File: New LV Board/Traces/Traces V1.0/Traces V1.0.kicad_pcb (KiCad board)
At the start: 2 copper layers, 126.6 x 49.2 mm, 15 parts, among them J1 B15B-PH-K-S, J2 B15B-PH-K-S, J3 B15B-PH-K-S, J4 Conn_01x12, J5 VBATT +, J6 Conn_01x12, J7 Conn_01x12, J8 Vs

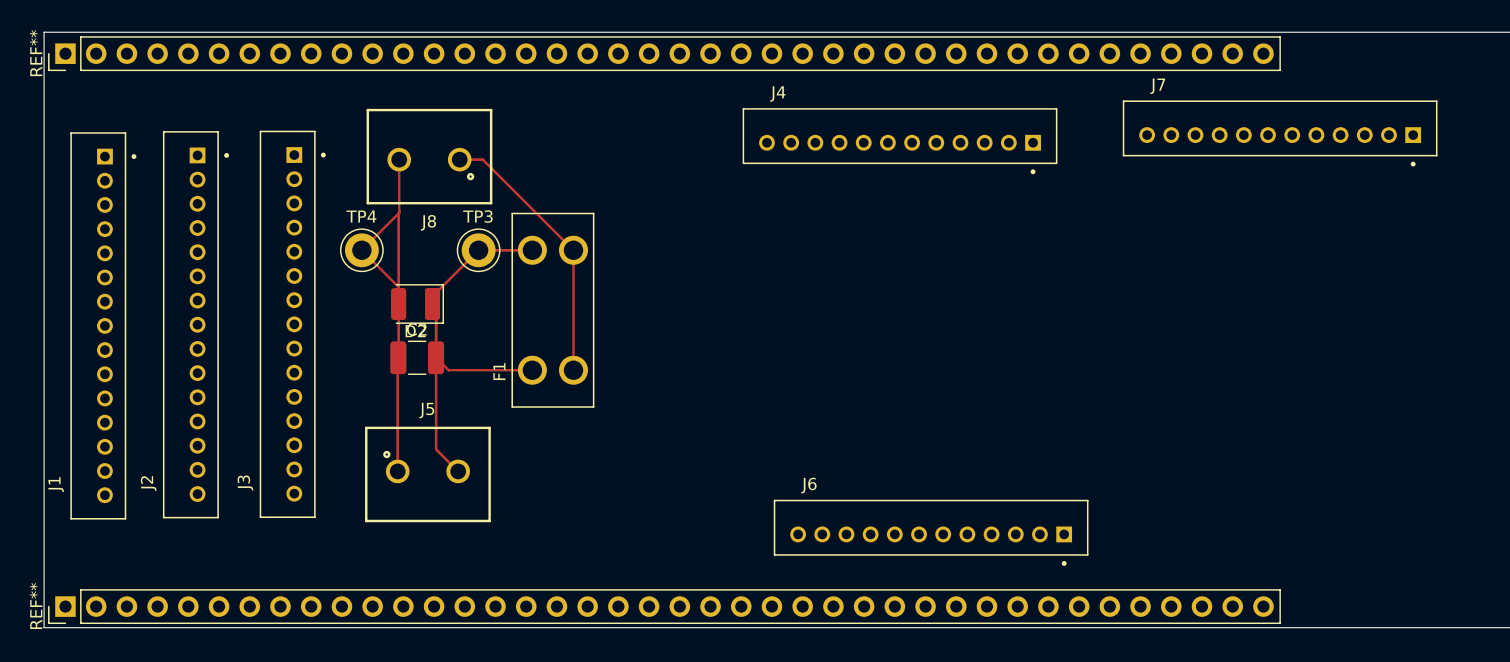
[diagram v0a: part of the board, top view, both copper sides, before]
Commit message: vcu throttle latching connected to traces
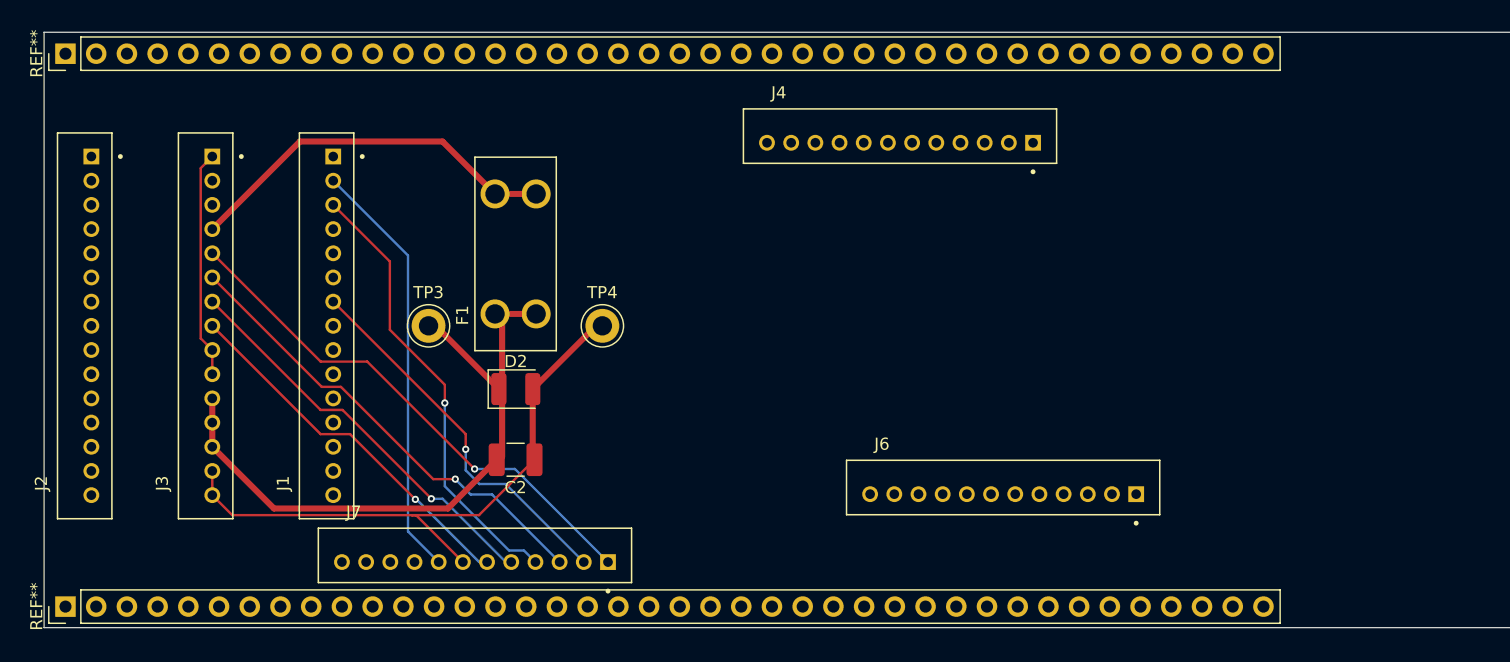
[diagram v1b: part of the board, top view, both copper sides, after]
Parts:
- removed J5: VBATT +, motorsports:691137710002
- removed J8: Vs, motorsports:691137710002
- moved J7 75.4 mm to (79.6, 138.3)
- moved TP4 20.8 mm to (90.1, 119.3)
- moved J1 18.9 mm to (67.3, 119.3)
- moved C2 11.7 mm to (82.9, 130.4), turned to 180 degrees
- moved D2 10.9 mm to (83.0, 124.5), turned to 0 degrees
- moved J2 8.78 mm to (47.3, 119.3)
- moved TP3 7.50 mm to (75.7, 119.3)
- moved J6 6.82 mm to (123.3, 132.6)
- moved J3 6.78 mm to (57.3, 119.3)
- moved F1 5.59 mm to (82.9, 113.3)
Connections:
- F1 pad 3: Net-(F1-Pad3) -> Net-(J4-Pin_3)
- F1 pad 4: Net-(F1-Pad3) -> Net-(J4-Pin_3)
- J1 pad 7: Net-(J7-Pin_6) -> Net-(J7-Pin_2)
- J3 pad 1: Net-(J7-Pin_5) -> Net-(J3-Pad1)
- J3 pad 10: unconnected-(J3-Pad10) -> Net-(J3-Pad1)
- J3 pad 11: unconnected-(J3-Pad11) -> Net-(D2-K)
- J3 pad 12: unconnected-(J3-Pad12) -> Net-(D2-K)
- J3 pad 13: unconnected-(J3-Pad13) -> Net-(D2-K)
- J3 pad 14: unconnected-(J3-Pad14) -> Net-(D2-A)
- J3 pad 15: unconnected-(J3-Pad15) -> Net-(D2-A)
- J3 pad 2: Net-(J4-Pin_3) -> unconnected-(J3-Pad2)
- J3 pad 4: Net-(J7-Pin_12) -> Net-(J4-Pin_3)
- J3 pad 5: Net-(J7-Pin_10) -> Net-(J7-Pin_1)
- J3 pad 6: unconnected-(J3-Pad6) -> Net-(J7-Pin_3)
- J3 pad 7: unconnected-(J3-Pad7) -> Net-(J7-Pin_5)
- J3 pad 8: unconnected-(J3-Pad8) -> Net-(J7-Pin_6)
- J3 pad 9: unconnected-(J3-Pad9) -> Net-(J3-Pad1)
- J4 pad 6: Net-(J4-Pin_6) -> Net-(D2-A)
- J4 pad 8: Net-(J4-Pin_6) -> Net-(D2-A)
- J6 pad 7: Net-(J4-Pin_6) -> Net-(D2-A)
- J7 pad 1: Net-(J4-Pin_10) -> Net-(J7-Pin_1)
- J7 pad 10: Net-(J7-Pin_10) -> unconnected-(J7-Pin_10-Pad10)
- J7 pad 12: Net-(J7-Pin_12) -> unconnected-(J7-Pin_12-Pad12)
- J7 pad 2: Net-(J4-Pin_10) -> Net-(J7-Pin_2)
- J7 pad 3: Net-(J4-Pin_6) -> Net-(J7-Pin_3)
- J7 pad 4: Net-(J7-Pin_10) -> Net-(J4-Pin_7)
- J7 pad 7: Net-(J4-Pin_10) -> Net-(D2-A)
- J7 pad 8: Net-(J4-Pin_7) -> Net-(J4-Pin_10)
- J7 pad 9: Net-(J4-Pin_6) -> unconnected-(J7-Pin_9-Pad9)
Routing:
- net Net-(J7-Pin_1): track 0.00 -> 43.5 mm, vias 0 -> 1
- net Net-(J7-Pin_3): track 0.00 -> 38.5 mm, vias 0 -> 1
- net Net-(J4-Pin_7): track 0.00 -> 37.2 mm, vias 0 -> 1
- net Net-(J4-Pin_10): track 0.00 -> 35.1 mm
- net Net-(J7-Pin_5): track 0.00 -> 33.6 mm, vias 0 -> 1
- net Net-(J4-Pin_3): track 0.00 -> 31.6 mm
- net Net-(J7-Pin_2): track 0.00 -> 31.4 mm, vias 0 -> 1
- net Net-(J7-Pin_6): track 0.00 -> 30.8 mm, vias 0 -> 1
- net Net-(F1-Pad3): track 22.4 -> 0.00 mm
- net Net-(J3-Pad1): track 0.00 -> 18.8 mm
- net Net-(D2-K): track 37.9 -> 55.0 mm
- net Net-(D2-A): track 35.9 -> 50.9 mm

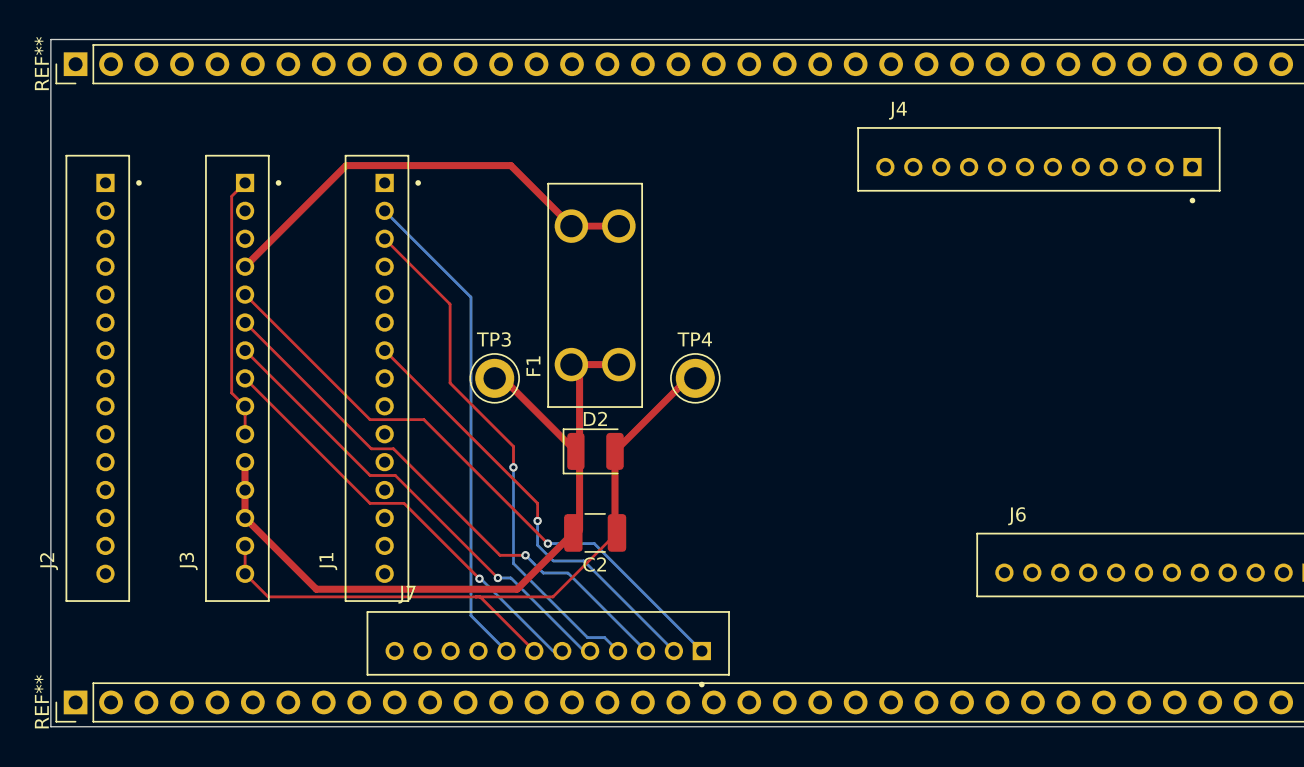
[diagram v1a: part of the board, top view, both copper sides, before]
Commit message: traces board changed to add VCU MPR - 5V connections
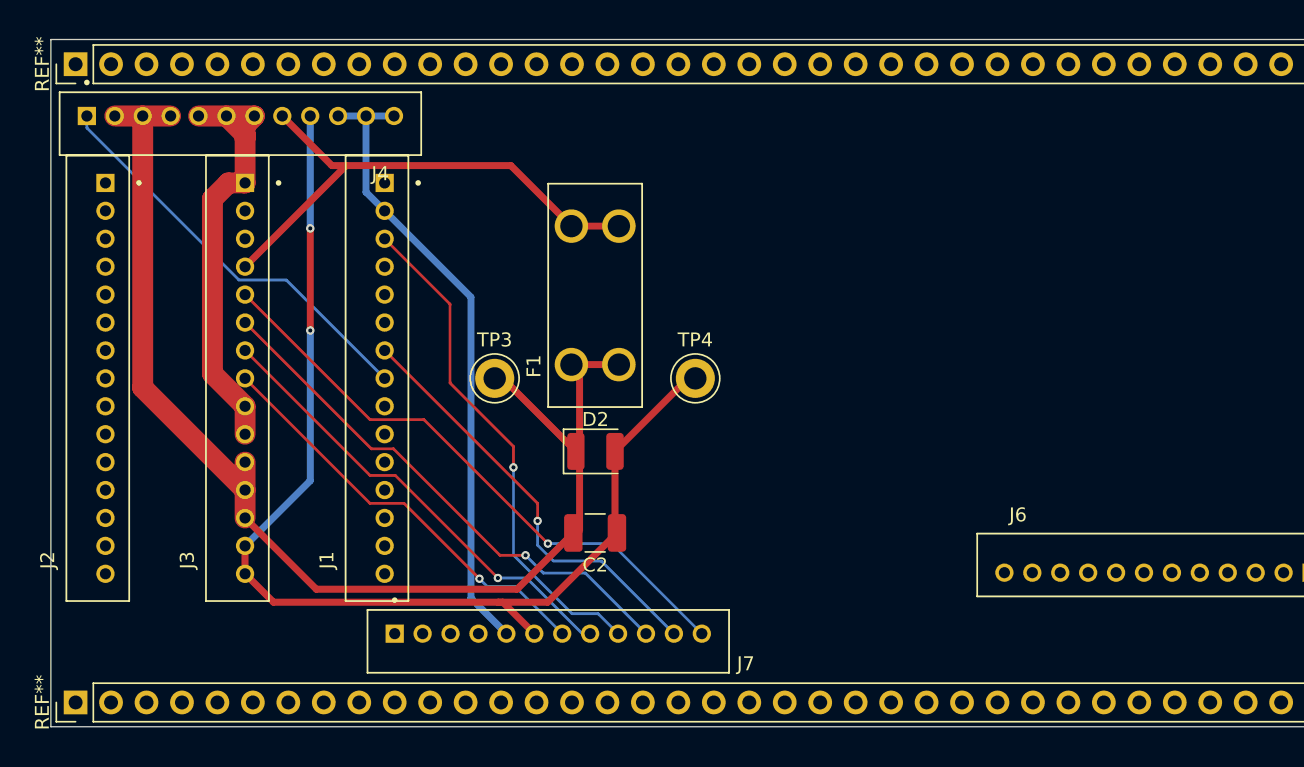
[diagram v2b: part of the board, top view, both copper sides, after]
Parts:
- moved J4 57.3 mm to (57.5, 101.0), turned to 180 degrees
- moved J7 0.14 mm to (79.6, 138.1), turned to 180 degrees
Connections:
- F1 pad 3: Net-(J4-Pin_3) -> Net-(J4-Pin_8)
- F1 pad 4: Net-(J4-Pin_3) -> Net-(J4-Pin_8)
- J1 pad 1: Net-(J4-Pin_4) -> Net-(J6-Pin_11)
- J1 pad 10: Net-(J4-Pin_1) -> Net-(J6-Pin_8)
- J1 pad 11: Net-(J4-Pin_2) -> Net-(J6-Pin_9)
- J1 pad 12: Net-(J6-Pin_5) -> Net-(J6-Pin_7)
- J1 pad 14: Net-(J6-Pin_2) -> Net-(J6-Pin_4)
- J1 pad 15: Net-(J6-Pin_3) -> Net-(J6-Pin_5)
- J1 pad 3: Net-(J4-Pin_7) -> Net-(J6-Pin_12)
- J1 pad 7: Net-(J7-Pin_2) -> Net-(J7-Pin_11)
- J1 pad 8: Net-(J6-Pin_1) -> Net-(J4-Pin_1)
- J1 pad 9: Net-(J4-Pin_5) -> Net-(J6-Pin_10)
- J3 pad 1: Net-(J3-Pad1) -> Net-(J4-Pin_5)
- J3 pad 10: Net-(J3-Pad1) -> Net-(J4-Pin_5)
- J3 pad 4: Net-(J4-Pin_3) -> Net-(J4-Pin_8)
- J3 pad 5: Net-(J7-Pin_1) -> Net-(J7-Pin_12)
- J3 pad 6: Net-(J7-Pin_3) -> Net-(J7-Pin_10)
- J3 pad 7: Net-(J7-Pin_5) -> Net-(J7-Pin_8)
- J3 pad 8: Net-(J7-Pin_6) -> Net-(J7-Pin_7)
- J3 pad 9: Net-(J3-Pad1) -> Net-(J4-Pin_5)
- J4 pad 2: Net-(J4-Pin_2) -> Net-(D2-K)
- J4 pad 3: Net-(J4-Pin_3) -> Net-(D2-K)
- J4 pad 4: Net-(J4-Pin_4) -> Net-(D2-K)
- J4 pad 6: Net-(D2-A) -> Net-(J4-Pin_5)
- J4 pad 7: Net-(J4-Pin_7) -> Net-(J4-Pin_5)
- J4 pad 8: Net-(D2-A) -> Net-(J4-Pin_8)
- J4 pad 9: Net-(J4-Pin_3) -> Net-(D2-A)
- J6 pad 1: Net-(J6-Pin_1) -> Net-(J4-Pin_5)
- J6 pad 10: unconnected-(J6-Pin_10-Pad10) -> Net-(J6-Pin_10)
- J6 pad 11: unconnected-(J6-Pin_11-Pad11) -> Net-(J6-Pin_11)
- J6 pad 12: unconnected-(J6-Pin_12-Pad12) -> Net-(J6-Pin_12)
- J6 pad 2: Net-(J6-Pin_2) -> Net-(J4-Pin_8)
- J6 pad 3: Net-(J6-Pin_3) -> Net-(D2-A)
- J6 pad 4: Net-(J4-Pin_3) -> Net-(J6-Pin_4)
- J6 pad 7: Net-(D2-A) -> Net-(J6-Pin_7)
- J6 pad 8: Net-(J4-Pin_7) -> Net-(J6-Pin_8)
- J6 pad 9: unconnected-(J6-Pin_9-Pad9) -> Net-(J6-Pin_9)
- J7 pad 1: Net-(J7-Pin_1) -> unconnected-(J7-Pin_1-Pad1)
- J7 pad 10: unconnected-(J7-Pin_10-Pad10) -> Net-(J7-Pin_10)
- J7 pad 11: unconnected-(J7-Pin_11-Pad11) -> Net-(J7-Pin_11)
- J7 pad 12: unconnected-(J7-Pin_12-Pad12) -> Net-(J7-Pin_12)
- J7 pad 2: Net-(J7-Pin_2) -> unconnected-(J7-Pin_2-Pad2)
- J7 pad 3: Net-(J7-Pin_3) -> unconnected-(J7-Pin_3-Pad3)
- J7 pad 4: Net-(J4-Pin_7) -> unconnected-(J7-Pin_4-Pad4)
- J7 pad 5: Net-(J7-Pin_5) -> Net-(J4-Pin_10)
- J7 pad 6: Net-(J7-Pin_6) -> Net-(D2-A)
- J7 pad 7: Net-(D2-A) -> Net-(J7-Pin_7)
- J7 pad 8: Net-(J4-Pin_10) -> Net-(J7-Pin_8)
- J7 pad 9: unconnected-(J7-Pin_9-Pad9) -> Net-(J6-Pin_12)
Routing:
- net Net-(J7-Pin_1): track 43.5 -> 0.00 mm, vias 1 -> 0
- net Net-(J7-Pin_12): track 0.00 -> 43.0 mm, vias 0 -> 1
- net Net-(J7-Pin_3): track 38.5 -> 0.00 mm, vias 1 -> 0
- net Net-(J7-Pin_10): track 0.00 -> 38.0 mm, vias 0 -> 1
- net Net-(J4-Pin_8): track 0.00 -> 37.6 mm
- net Net-(J4-Pin_7): track 37.2 -> 0.00 mm, vias 1 -> 0
- net Net-(J6-Pin_12): track 0.00 -> 36.3 mm, vias 0 -> 1
- net Net-(D2-K): track 55.0 -> 88.8 mm
- net Net-(J7-Pin_5): track 33.6 -> 0.00 mm, vias 1 -> 0
- net Net-(J7-Pin_8): track 0.00 -> 33.1 mm, vias 0 -> 1
- net Net-(J4-Pin_5): track 0.00 -> 31.8 mm
- net Net-(J4-Pin_3): track 31.6 -> 0.00 mm
- net Net-(J7-Pin_2): track 31.4 -> 0.00 mm, vias 1 -> 0
- net Net-(J7-Pin_11): track 0.00 -> 30.9 mm, vias 0 -> 1
- net Net-(J7-Pin_6): track 30.8 -> 0.00 mm, vias 1 -> 0
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
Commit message: TRACES IS DONE
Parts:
- moved J6 35.2 mm to (108.4, 100.8), turned to 180 degrees
- moved J1 20.1 mm to (47.3, 121.3)
- moved J2 20.1 mm to (67.3, 121.3)
- moved REF** 5.08 mm to (45.7, 147.6)
- moved J7 4.90 mm to (79.6, 143.0)
- moved D2 2.02 mm to (83.0, 126.5)
- moved F1 2.02 mm to (82.9, 115.4)
- moved C2 2.02 mm to (82.9, 132.4)
- moved J3 2.02 mm to (57.3, 121.3)
- moved TP3 2.02 mm to (75.7, 121.3)
- moved TP4 2.02 mm to (90.1, 121.3)
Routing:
- net Net-(J6-Pin_10): track 0.00 -> 116.7 mm
- net Net-(J6-Pin_9): track 0.00 -> 106.5 mm, vias 0 -> 2
- net Net-(J6-Pin_8): track 0.00 -> 105.3 mm, vias 0 -> 2
- net Net-(J6-Pin_12): track 36.3 -> 130.9 mm, vias 1 -> 0
- net Net-(J6-Pin_7): track 0.00 -> 88.8 mm, vias 0 -> 1
- net Net-(J6-Pin_6): track 0.00 -> 87.4 mm, vias 0 -> 1
- net Net-(J6-Pin_5): track 0.00 -> 86.8 mm, vias 0 -> 1
- net Net-(J6-Pin_4): track 0.00 -> 82.9 mm, vias 0 -> 1
- net Net-(J6-Pin_11): track 0.00 -> 81.4 mm
- net Net-(J4-Pin_5): track 31.8 -> 72.6 mm
- net Net-(J4-Pin_10): track 45.2 -> 81.6 mm, vias 0 -> 2
- net Net-(J7-Pin_11): track 30.9 -> 63.1 mm
- net Net-(D2-A): track 81.6 -> 111.8 mm, vias 2 -> 1
- net Net-(J7-Pin_10): track 38.0 -> 67.6 mm, vias 1 -> 0
- net Net-(J7-Pin_12): track 43.0 -> 66.6 mm, vias 1 -> 2
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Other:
- board size 126.6 x 49.2 mm -> 103.1 x 54.3 mm

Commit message: rotated JST PH 12 it may not match the schematic exactly but it is correct electrically.
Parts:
- moved J7 1.02 mm to (79.6, 142.0), turned to 0 degrees
- moved J1 0.98 mm to (48.3, 121.3), turned to -90 degrees
- moved J3 0.98 mm to (58.3, 121.3), turned to -90 degrees
- moved J2 0.98 mm to (68.3, 121.3), turned to -90 degrees
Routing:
- net Net-(J4-Pin_5): track 72.6 -> 179.8 mm
- net Net-(J7-Pin_10): track 67.6 -> 0.00 mm
- net Net-(J7-Pin_12): track 66.6 -> 0.00 mm, vias 2 -> 0
- net Net-(D2-K): track 90.0 -> 156.6 mm, vias 0 -> 2
- net Net-(J7-Pin_8): track 39.5 -> 0.00 mm

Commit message: No significant changes just random kicad BS
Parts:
- moved D2 5.91 mm to (85.5, 121.2)
- moved F1 5.91 mm to (85.5, 110.0)
- moved J6 5.91 mm to (110.9, 95.5)
- moved J7 5.91 mm to (82.1, 136.7)
- moved REF** 5.91 mm to (48.3, 142.2)
- moved REF** 5.91 mm to (48.3, 91.4)
- moved C2 5.91 mm to (85.5, 127.0)
- moved J2 5.91 mm to (70.8, 116.0)
- moved TP4 5.91 mm to (92.7, 116.0)
- moved J1 5.91 mm to (50.8, 116.0)
- moved J3 5.91 mm to (60.8, 116.0)
- moved J4 5.91 mm to (60.1, 95.7)
- moved TP3 5.91 mm to (78.3, 116.0)
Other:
- board size 103.1 x 54.3 mm -> 103.1 x 53.3 mm

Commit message: Gerbers for Traces board
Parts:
- moved D2 5.91 mm to (83.0, 126.5)
- moved F1 5.91 mm to (82.9, 115.4)
- moved J6 5.91 mm to (108.4, 100.8)
- moved J7 5.91 mm to (79.6, 142.0)
- moved REF** 5.91 mm to (45.7, 147.6)
- moved REF** 5.91 mm to (45.7, 96.8)
- moved C2 5.91 mm to (82.9, 132.4)
- moved J2 5.91 mm to (68.3, 121.3)
- moved TP4 5.91 mm to (90.1, 121.3)
- moved J1 5.91 mm to (48.3, 121.3)
- moved J3 5.91 mm to (58.3, 121.3)
- moved J4 5.91 mm to (57.5, 101.0)
- moved TP3 5.91 mm to (75.7, 121.3)
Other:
- board size 103.1 x 53.3 mm -> 103.1 x 54.3 mm
- board text added: "Traces V1.0 | J.E. Nov '25"

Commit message: traces fixing pt 1
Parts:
- removed REF** (x2): PinHeader_1x40_P2.54mm_Vertical, Connector_PinHeader_2.54mm:PinHeader_1x40_P2.54mm_Vertical
- moved J6 77.1 mm to (170.6, 55.3), turned to 0 degrees
- moved J4 74.5 mm to (116.4, 55.3), turned to 0 degrees
- moved C2 70.6 mm to (128.8, 78.7), turned to 0 degrees
- moved J7 69.5 mm to (140.5, 108.5), turned to 180 degrees
- moved TP3 63.6 mm to (123.3, 79.1)
- moved D2 63.4 mm to (130.9, 85.1)
- moved F1 63.4 mm to (129.5, 72.4), turned to 0 degrees
- moved TP4 49.8 mm to (123.3, 84.1)
- moved J3 47.5 mm to (83.1, 80.7)
- moved J2 47.2 mm to (94.5, 82.0)
- moved J1 46.3 mm to (71.7, 81.3)
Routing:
- net Net-(J4-Pin_5): track 179.8 -> 0.00 mm
- net Net-(D2-K): track 156.6 -> 0.00 mm, vias 2 -> 0
- net Net-(J6-Pin_12): track 130.9 -> 0.00 mm
- net Net-(J6-Pin_10): track 116.7 -> 0.00 mm
- net Net-(D2-A): track 111.8 -> 0.00 mm, vias 1 -> 0
- net Net-(J6-Pin_9): track 106.5 -> 0.00 mm, vias 2 -> 0
- net Net-(J6-Pin_8): track 105.3 -> 0.00 mm, vias 2 -> 0
- net Net-(J6-Pin_7): track 88.8 -> 0.00 mm, vias 1 -> 0
- net Net-(J6-Pin_6): track 87.4 -> 0.00 mm, vias 1 -> 0
- net Net-(J6-Pin_5): track 86.8 -> 0.00 mm, vias 1 -> 0
- net Net-(J6-Pin_4): track 82.9 -> 0.00 mm, vias 1 -> 0
- net Net-(J4-Pin_10): track 81.6 -> 0.00 mm, vias 2 -> 0
- net Net-(J6-Pin_11): track 81.4 -> 0.00 mm
- net Net-(J7-Pin_11): track 63.1 -> 0.00 mm, vias 1 -> 0
- net Net-(J4-Pin_8): track 60.0 -> 0.00 mm
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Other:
- board size 103.1 x 54.3 mm -> 103.1 x 51.8 mm

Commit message: Traces V1.0
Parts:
- added REF**: PinHeader_1x20_P2.54mm_Vertical, Connector_PinHeader_2.54mm:PinHeader_1x20_P2.54mm_Vertical, F.Cu at (40.6, 61.0)
- added REF**: PinHeader_1x20_P2.54mm_Vertical, Connector_PinHeader_2.54mm:PinHeader_1x20_P2.54mm_Vertical, F.Cu at (40.6, 109.2)
- added REF**: PinHeader_1x20_P2.54mm_Vertical, Connector_PinHeader_2.54mm:PinHeader_1x20_P2.54mm_Vertical, F.Cu at (92.7, 61.0)
- added REF**: PinHeader_1x20_P2.54mm_Vertical, Connector_PinHeader_2.54mm:PinHeader_1x20_P2.54mm_Vertical, F.Cu at (92.7, 109.2)
- moved J4 62.8 mm to (54.9, 68.0)
- moved J6 60.1 mm to (112.1, 68.9)
- moved J7 52.4 mm to (88.5, 102.2)
- moved TP3 40.7 mm to (83.0, 85.1)
- moved TP4 40.7 mm to (83.0, 90.1)
- moved F1 40.7 mm to (89.3, 78.4)
- moved D2 40.3 mm to (91.0, 90.6)
- moved C2 38.2 mm to (91.1, 84.8)
- moved J2 30.6 mm to (64.5, 87.9)
- moved J3 29.4 mm to (54.5, 87.9)
- moved J1 27.7 mm to (44.8, 88.0)
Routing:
- net Net-(J7-Pin_8): track 0.00 -> 102.4 mm
- net Net-(J7-Pin_7): track 0.00 -> 97.8 mm
- net Net-(D2-A): track 0.00 -> 87.3 mm, vias 0 -> 1
- net Net-(J7-Pin_11): track 0.00 -> 83.0 mm
- net Net-(J4-Pin_8): track 0.00 -> 73.1 mm, vias 0 -> 1
- net Net-(J7-Pin_12): track 0.00 -> 56.2 mm
- net Net-(J7-Pin_10): track 0.00 -> 52.8 mm
- net Net-(J6-Pin_12): track 0.00 -> 35.3 mm
- net Net-(J4-Pin_10): track 0.00 -> 34.5 mm
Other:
- board size 103.1 x 51.8 mm -> 105.7 x 51.8 mm
- board text added: "J4"
- board text removed: "Traces V1.0 | J.E. Nov '25"
